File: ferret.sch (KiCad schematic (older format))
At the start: 0 parts

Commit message: Add some part numbers, more changes
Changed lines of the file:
@@
 F9 "~INT_PMC" O R 3350 3750 50
 F10 "EN_SINK" I R 3350 4000 50
+F11 "ACDRV1" I R 3350 3450 50
+F12 "VAC1" I R 3350 3350 50
 $EndSheet
 $Sheet
@@
 F6 "SDA" B R 6200 3250 50
 F7 "~CE" I R 6200 3450 50
+F8 "VAC1" I L 4650 3350 50
+F9 "ACDRV1" I L 4650 3450 50
 $EndSheet
 $Sheet
@@
 Wire Wire Line
 	4300 3750 3350 3750
+Wire Wire Line
+	4650 3450 3350 3450
+Wire Wire Line
+	3350 3350 4650 3350
 $EndSCHEMATC

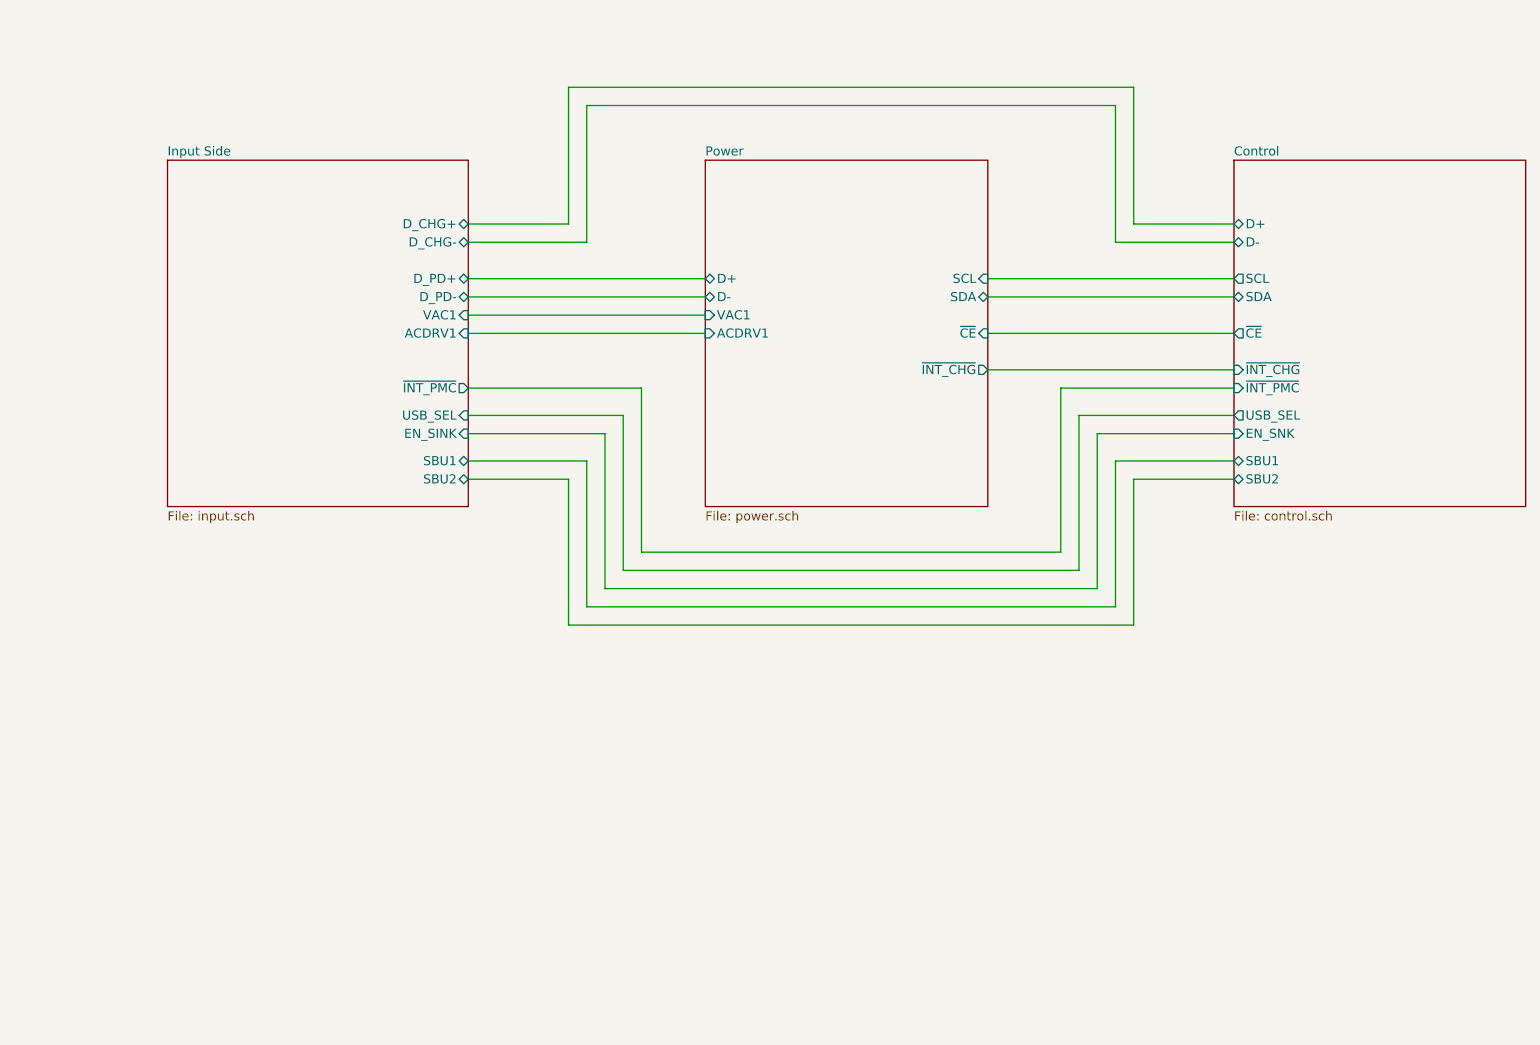
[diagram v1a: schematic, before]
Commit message: placed to 50x50mm, started to route
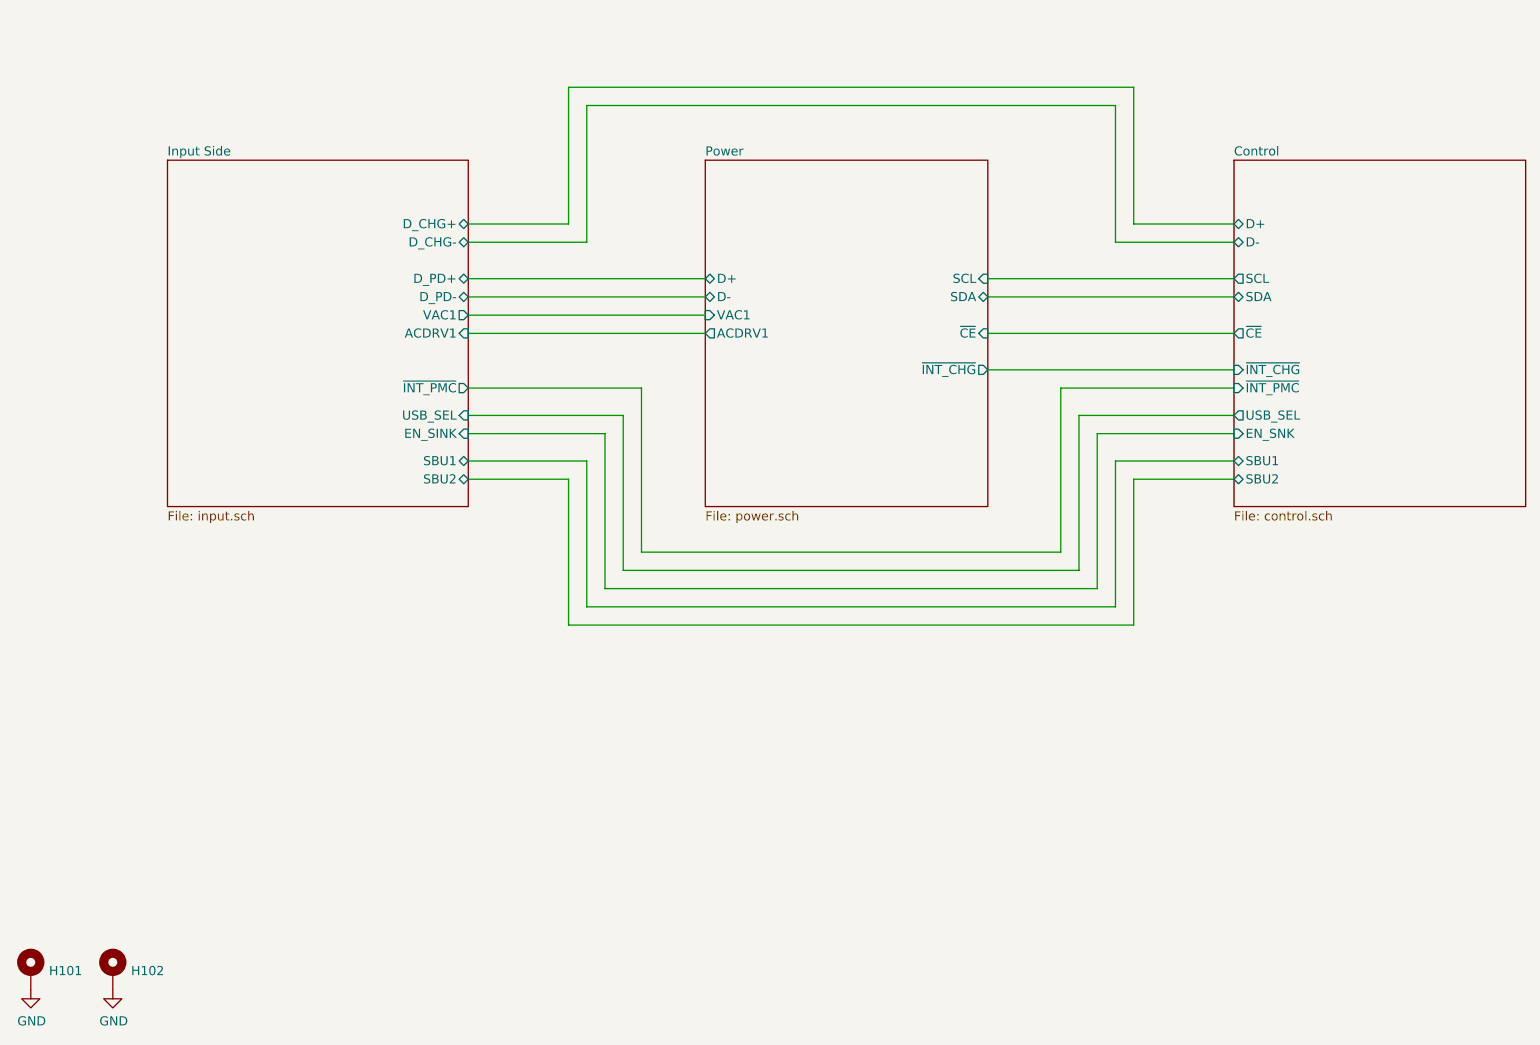
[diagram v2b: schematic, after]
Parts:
- added H101, H102: MountingHole_Pad, MountingHole:MountingHole_3.2mm_M3_ISO14580_Pad, symbol Mechanical:MountingHole_Pad
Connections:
- new net GND: H101.1, H102.1
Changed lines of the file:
@@
 F10 "EN_SINK" I R 3350 4000 50
 F11 "ACDRV1" I R 3350 3450 50
-F12 "VAC1" I R 3350 3350 50
+F12 "VAC1" O R 3350 3350 50
 $EndSheet
 $Sheet
@@
 F7 "~CE" I R 6200 3450 50
 F8 "VAC1" I L 4650 3350 50
-F9 "ACDRV1" I L 4650 3450 50
+F9 "ACDRV1" O L 4650 3450 50
 $EndSheet
 $Sheet
@@
 Wire Wire Line
 	3350 3350 4650 3350
+$Comp
+L Mechanical:MountingHole_Pad H102
+U 1 1 5F8E13F6
+P 1400 6950
+F 0 "H102" H 1500 6953 50  0000 L CNN
+F 1 "MountingHole_Pad" H 1500 6908 50  0001 L CNN
+F 2 "MountingHole:MountingHole_3.2mm_M3_ISO14580_Pad" H 1400 6950 50  0001 C CNN
+F 3 "~" H 1400 6950 50  0001 C CNN
+F 4 "DNP" H 1400 6950 50  0001 C CNN "MPN"
+	1    1400 6950
+	1    0    0    -1
+$EndComp
+$Comp
+L power:GND #PWR0116
+U 1 1 5F8E1B2F
+P 1400 7050
+F 0 "#PWR0116" H 1400 6800 50  0001 C CNN
+F 1 "GND" H 1405 6877 50  0000 C CNN
+F 2 "" H 1400 7050 50  0001 C CNN
+F 3 "" H 1400 7050 50  0001 C CNN
+	1    1400 7050
+	1    0    0    -1
+$EndComp
+$Comp
+L Mechanical:MountingHole_Pad H101
+U 1 1 5F8E4BF3
+P 950 6950
+F 0 "H101" H 1050 6953 50  0000 L CNN
+F 1 "MountingHole_Pad" H 1050 6908 50  0001 L CNN
+F 2 "MountingHole:MountingHole_3.2mm_M3_ISO14580_Pad" H 950 6950 50  0001 C CNN
+F 3 "~" H 950 6950 50  0001 C CNN
+F 4 "DNP" H 950 6950 50  0001 C CNN "MPN"
+	1    950  6950
+	1    0    0    -1
+$EndComp
+$Comp
+L power:GND #PWR0115
+U 1 1 5F8E4BF9
+P 950 7050
+F 0 "#PWR0115" H 950 6800 50  0001 C CNN
+F 1 "GND" H 955 6877 50  0000 C CNN
+F 2 "" H 950 7050 50  0001 C CNN
+F 3 "" H 950 7050 50  0001 C CNN
+	1    950  7050
+	1    0    0    -1
+$EndComp
 $EndSCHEMATC

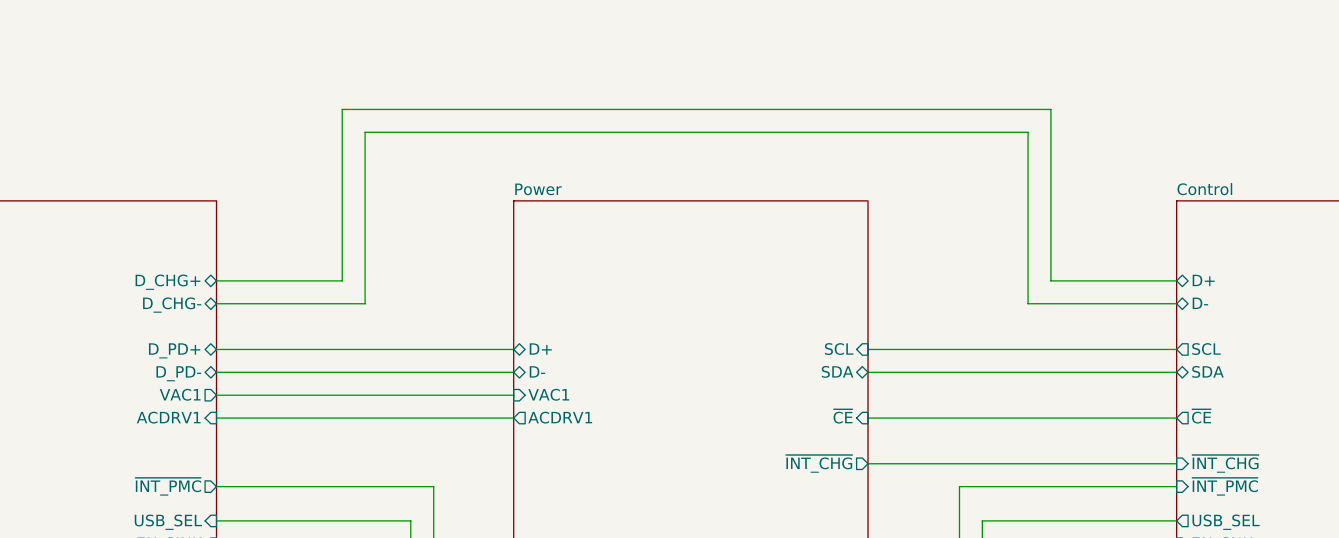
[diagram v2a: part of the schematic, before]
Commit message: fully routed but silk is still not done
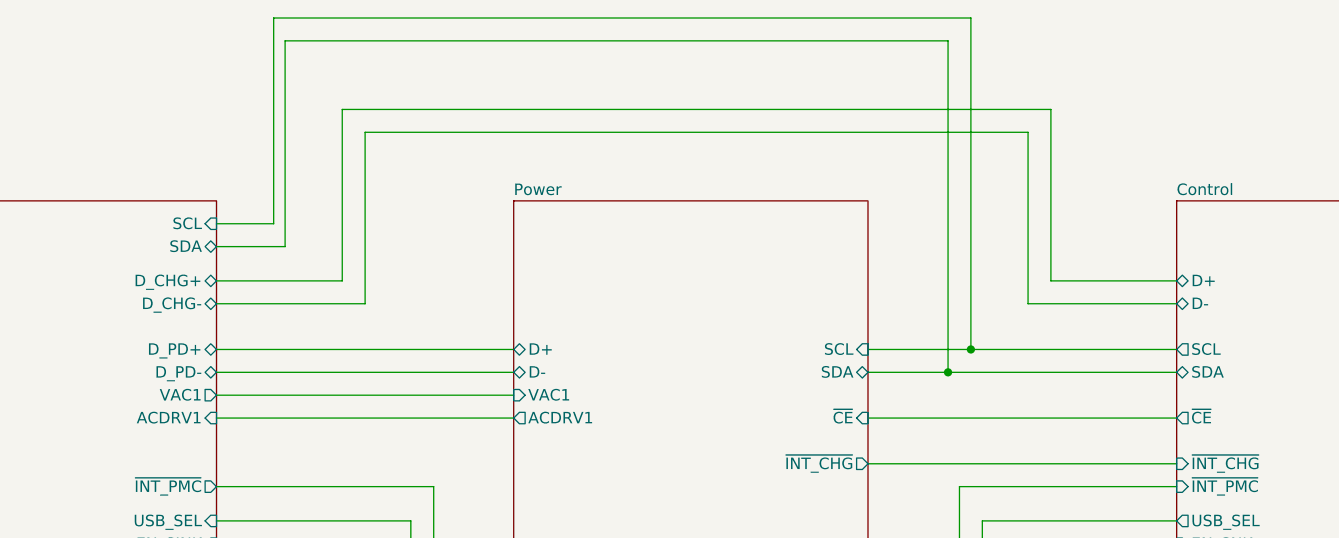
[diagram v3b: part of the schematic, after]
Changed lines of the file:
@@
 F11 "ACDRV1" I R 3350 3450 50
 F12 "VAC1" O R 3350 3350 50
+F13 "SCL" I R 3350 2600 50
+F14 "SDA" B R 3350 2700 50
 $EndSheet
 $Sheet
@@
 $EndSheet
 Wire Wire Line
-	6200 3250 7550 3250
+	6200 3250 6550 3250
 Wire Wire Line
-	7550 3150 6200 3150
+	7550 3150 6650 3150
 Wire Wire Line
 	7550 3450 6200 3450
@@
 	1    0    0    -1
 $EndComp
+Wire Wire Line
+	3350 2600 3600 2600
+Wire Wire Line
+	3600 2600 3600 1700
+Wire Wire Line
+	3600 1700 6650 1700
+Wire Wire Line
+	6650 1700 6650 3150
+Connection ~ 6650 3150
+Wire Wire Line
+	6650 3150 6200 3150
+Wire Wire Line
+	6550 3250 6550 1800
+Wire Wire Line
+	6550 1800 3650 1800
+Wire Wire Line
+	3650 1800 3650 2700
+Wire Wire Line
+	3650 2700 3350 2700
+Connection ~ 6550 3250
+Wire Wire Line
+	6550 3250 7550 3250
 $EndSCHEMATC
